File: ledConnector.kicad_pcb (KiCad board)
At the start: 2 copper layers, 30 x 15.5 mm, 7 parts, among them J1 Conn_01x06_Pin, J2 Conn_01x01_Pin, J3 Conn_01x01_Pin, J4 Conn_01x01_Pin, J5 Conn_01x01_Pin, J6 Conn_01x01_Pin, J7 Conn_01x01_Pin

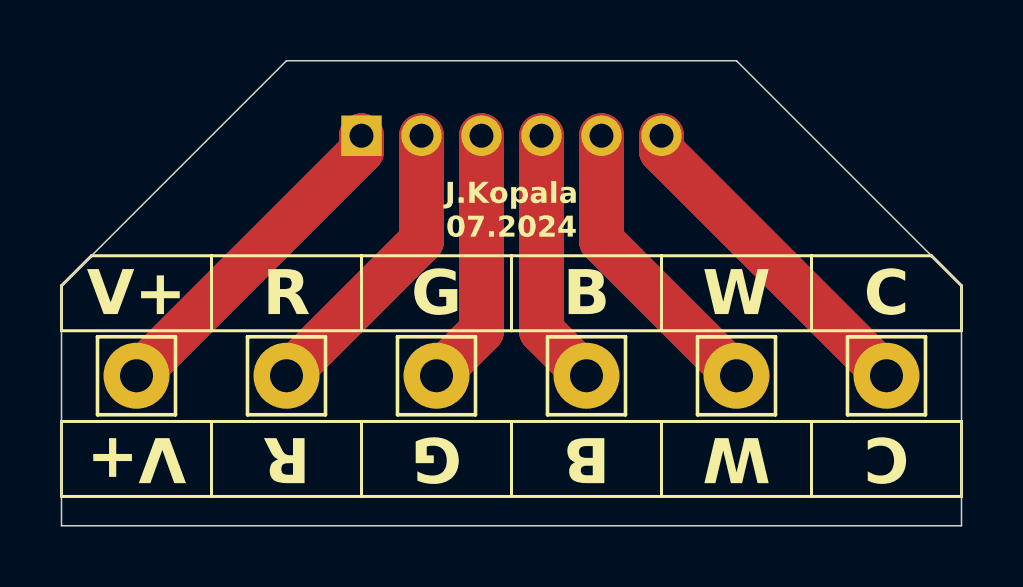
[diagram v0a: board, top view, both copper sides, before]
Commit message: fix(PCB): Change pin mapping
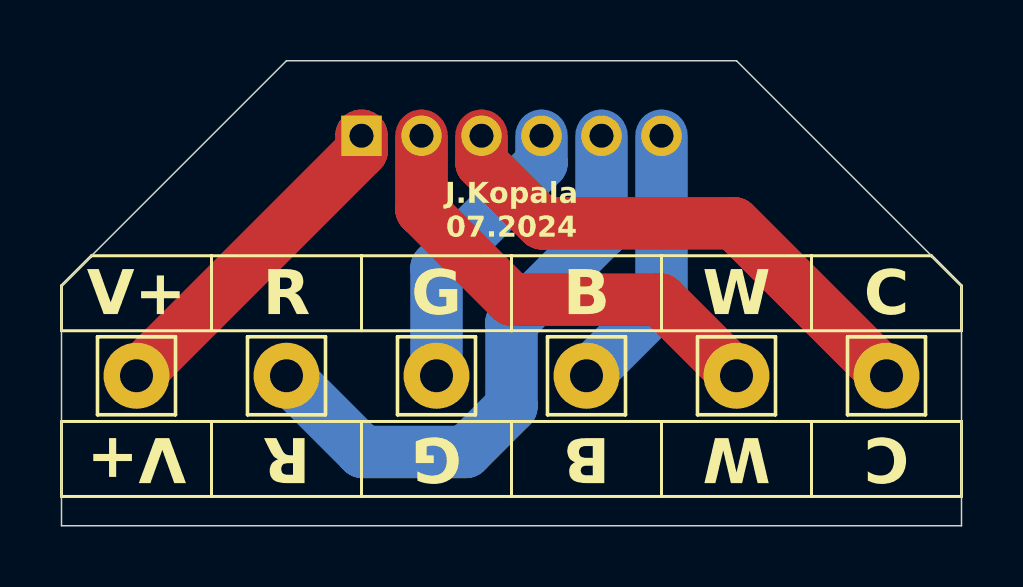
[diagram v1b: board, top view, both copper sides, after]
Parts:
- moved J3 15.0 mm to (156.0, 109.0)
- moved J4 15.0 mm to (161.0, 109.0)
- moved J6 15.0 mm to (141.0, 109.0)
- moved J7 10.0 mm to (151.0, 109.0)
- moved J5 5.00 mm to (146.0, 109.0)
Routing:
- net Net-(J1-Pin_6): track 22.2 -> 9.04 mm
- net Net-(J1-Pin_4): track 17.2 -> 9.45 mm
- net Net-(J1-Pin_2): track 19.7 -> 15.6 mm
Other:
- board text added: "LED_Connector V2.0"
- board text removed: "LED_Connector V1.0"
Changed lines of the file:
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@@
 	(footprint "Connector_Pin:Pin_D1.1mm_L8.5mm_W2.5mm_FlatFork"
 		(layer "F.Cu")
-		(at 141 109 90)
+		(at 156 109 90)
 		(descr "solder Pin_ with flat fork, hole diameter 1.1mm, length 8.5mm, width 2.5mm")
 		(tags "solder Pin_ with flat fork")
@@
 	(footprint "Connector_Pin:Pin_D1.1mm_L8.5mm_W2.5mm_FlatFork"
 		(layer "F.Cu")
-		(at 161 109 90)
+		(at 151 109 90)
 		(descr "solder Pin_ with flat fork, hole diameter 1.1mm, length 8.5mm, width 2.5mm")
 		(tags "solder Pin_ with flat fork")
@@
 	(footprint "Connector_Pin:Pin_D1.1mm_L8.5mm_W2.5mm_FlatFork"
 		(layer "F.Cu")
-		(at 151 109 90)
+		(at 146 109 90)
 		(descr "solder Pin_ with flat fork, hole diameter 1.1mm, length 8.5mm, width 2.5mm")
 		(tags "solder Pin_ with flat fork")
@@
 	(footprint "Connector_Pin:Pin_D1.1mm_L8.5mm_W2.5mm_FlatFork"
 		(layer "F.Cu")
-		(at 146 109 90)
+		(at 161 109 90)
 		(descr "solder Pin_ with flat fork, hole diameter 1.1mm, length 8.5mm, width 2.5mm")
 		(tags "solder Pin_ with flat fork")
@@
 	(footprint "Connector_Pin:Pin_D1.1mm_L8.5mm_W2.5mm_FlatFork"
 		(layer "F.Cu")
-		(at 156 109 90)
+		(at 141 109 90)
 		(descr "solder Pin_ with flat fork, hole diameter 1.1mm, length 8.5mm, width 2.5mm")
 		(tags "solder Pin_ with flat fork")
@@
 	)
 	(gr_text "C"
-		(at 160.692 106.27 0)
+		(at 161 106.27 0)
 		(layer "B.SilkS")
 		(effects
@@
 		)
 	)
-	(gr_text "LED_Connector\nV1.0"
+	(gr_text "LED_Connector\nV2.0"
 		(at 148.5 103.476 0)
 		(layer "B.SilkS")
@@
 	)
 	(segment
-		(start 153.5 101.5)
-		(end 161 109)
-		(width 1.5)
-		(layer "F.Cu")
-		(net 1)
-	)
-	(segment
-		(start 153.5 101)
-		(end 153.5 101.5)
-		(width 1.5)
-		(layer "F.Cu")
-		(net 1)
-	)
-	(segment
-		(start 161 109)
-		(end 153.5 101.5)
-		(width 1.5)
+		(start 151 109)
+		(end 153.5 106.5)
+		(width 1.75)
 		(layer "B.Cu")
 		(net 1)
 	)
 	(segment
-		(start 153.5 101.5)
+		(start 153.5 106.5)
 		(end 153.5 101)
-		(width 1.5)
+		(width 1.75)
 		(layer "B.Cu")
 		(net 1)
 	)
 	(segment
-		(start 145.5 101)
-		(end 145.5 104.5)
-		(width 1.5)
+		(start 156 108.626)
+		(end 156 109)
+		(width 0.2)
 		(layer "F.Cu")
 		(net 2)
 	)
 	(segment
-		(start 145.5 104.5)
-		(end 141 109)
-		(width 1.5)
+		(start 156 109)
+		(end 153.46 106.46)
+		(width 1.75)
 		(layer "F.Cu")
 		(net 2)
 	)
 	(segment
-		(start 141 109)
-		(end 145.5 104.5)
-		(width 1.5)
-		(layer "B.Cu")
+		(start 153.46 106.46)
+		(end 148.5 106.46)
+		(width 1.75)
+		(layer "F.Cu")
 		(net 2)
 	)
 	(segment
-		(start 145.5 104.5)
+		(start 145.5 103.46)
 		(end 145.5 101)
-		(width 1.5)
-		(layer "B.Cu")
+		(width 1.75)
+		(layer "F.Cu")
+		(net 2)
+	)
+	(segment
+		(start 148.5 106.46)
+		(end 145.5 103.46)
+		(width 1.75)
+		(layer "F.Cu")
 		(net 2)
 	)
@@
 		(start 143.5 101.5)
 		(end 136 109)
-		(width 1.5)
+		(width 1.75)
 		(layer "F.Cu")
 		(net 3)
@@
 		(start 143.5 101)
 		(end 143.5 101.5)
-		(width 1.5)
+		(width 1.75)
 		(layer "F.Cu")
 		(net 3)
@@
 		(start 143.5 101)
 		(end 143.5 101.5)
-		(width 1.5)
+		(width 1.75)
 		(layer "B.Cu")
 		(net 3)
@@
 		(start 143.5 101.5)
 		(end 136 109)
-		(width 1.5)
+		(width 1.75)
 		(layer "B.Cu")
 		(net 3)
 	)
 	(segment
-		(start 151.5 104.5)
-		(end 156 109)
-		(width 1.5)
-		(layer "F.Cu")
+		(start 148.5 110.016)
+		(end 146.976 111.54)
+		(width 1.75)
+		(layer "B.Cu")
+		(net 4)
+	)
+	(segment
+		(start 148.5 107.222)
+		(end 148.5 110.016)
+		(width 1.75)
+		(layer "B.Cu")
+		(net 4)
+	)
+	(segment
+		(start 146.976 111.54)
+		(end 143.54 111.54)
+		(width 1.75)
+		(layer "B.Cu")
 		(net 4)
 	)
 	(segment
 		(start 151.5 101)
-		(end 151.5 104.5)
-		(width 1.5)
-		(layer "F.Cu")
-		(net 4)
-	)
-	(segment
-		(start 151.5 104.5)
-		(end 151.5 101)
-		(width 1.5)
+		(end 151.5 104.222)
+		(width 1.75)
 		(layer "B.Cu")
 		(net 4)
 	)
 	(segment
-		(start 156 109)
-		(end 151.5 104.5)
-		(width 1.5)
+		(start 143.54 111.54)
+		(end 141 109)
+		(width 1.75)
 		(layer "B.Cu")
 		(net 4)
 	)
 	(segment
+		(start 151.5 104.222)
+		(end 148.5 107.222)
+		(width 1.75)
+		(layer "B.Cu")
+		(net 4)
+	)
+	(segment
 		(start 149.5 101)
-		(end 149.5 107.5)
-		(width 1.5)
-		(layer "F.Cu")
-		(net 5)
-	)
-	(segment
-		(start 149.5 107.5)
-		(end 151 109)
-		(width 1.5)
-		(layer "F.Cu")
-		(net 5)
-	)
-	(segment
-		(start 149.5 107.5)
-		(end 149.5 101)
-		(width 1.5)
+		(end 149.5 101.904)
+		(width 1.75)
 		(layer "B.Cu")
 		(net 5)
 	)
 	(segment
-		(start 151 109)
-		(end 149.5 107.5)
-		(width 1.5)
+		(start 149.5 101.904)
+		(end 146 105.404)
+		(width 1.75)
 		(layer "B.Cu")
 		(net 5)
 	)
 	(segment
-		(start 147.5 107.5)
+		(start 146 105.404)
 		(end 146 109)
-		(width 1.5)
+		(width 1.75)
+		(layer "B.Cu")
+		(net 5)
+	)
+	(segment
+		(start 155.92 103.92)
+		(end 161 109)
+		(width 1.75)
 		(layer "F.Cu")
 		(net 6)
 	)
 	(segment
-		(start 147.5 101)
-		(end 147.5 107.5)
-		(width 1.5)
+		(start 149.516 103.92)
+		(end 155.92 103.92)
+		(width 1.75)
 		(layer "F.Cu")
 		(net 6)
 	)
 	(segment
-		(start 146 109)
-		(end 147.5 107.5)
-		(width 1.5)
-		(layer "B.Cu")
+		(start 147.5 101.904)
+		(end 149.516 103.92)
+		(width 1.75)
+		(layer "F.Cu")
 		(net 6)
 	)
 	(segment
-		(start 147.5 107.5)
-		(end 147.5 101)
-		(width 1.5)
-		(layer "B.Cu")
+		(start 147.5 101)
+		(end 147.5 101.904)
+		(width 1.75)
+		(layer "F.Cu")
 		(net 6)
 	)
